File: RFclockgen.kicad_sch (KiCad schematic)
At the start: 13 parts, among them J1 Conn_01x04_Pin, J3 Conn_01x02_Pin, U3 AP2112K-3.3, U4 ESP32-C6-WROOM-1-N8

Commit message: restored to an older version
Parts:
- removed C11: 0.1u, symbol Device:C
- removed C12: 1u, symbol Device:C
- removed R10: 10k, symbol Device:R
- added C2: 10pF, Capacitor_SMD:C_0603_1608Metric_Pad1.08x0.95mm_HandSolder, symbol Device:C
- added R1, R2, R3: 51, Resistor_SMD:R_0603_1608Metric_Pad0.98x0.95mm_HandSolder, symbol Device:R
- added XTAL1: SIT1552AI-JF-DCC-32.768D, BGA4_SiT1532_SIT, symbol 2026-10-07_02-35-18:SIT1552AI-JF-DCC-32.768D
- C5: value 0.1u -> 12p
- C6: value 22u -> 12p
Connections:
- net 3.3V: now also R1.1; no longer C6.1
- net EN: no longer C5.2
- net GND: now also C5.2, R3.2, XTAL1.1 (GND), XTAL1.4 (GND); no longer C5.1
- net at U4.8 (IO0): now also C6.1, XTAL1.2 (CLK_OUT)
- net at U4.9 (IO1): now also C5.1, XTAL1.3 (VDD)
- new net: R1.2, R2.1
- new net: C2.1, R3.1
- new net RF_OUT_A-: C2.2, R2.2
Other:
- removed sheet #PWR020
- added sheet Decoupling capacitors (untitled.kicad_sch)

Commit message: Update
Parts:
- removed C2: 10pF, Capacitor_SMD:C_0603_1608Metric_Pad1.08x0.95mm_HandSolder, symbol Device:C
- removed R1, R2, R3: 51, Resistor_SMD:R_0603_1608Metric_Pad0.98x0.95mm_HandSolder, symbol Device:R
- removed XTAL1: SIT1552AI-JF-DCC-32.768D, BGA4_SiT1532_SIT, symbol 2026-10-07_02-35-18:SIT1552AI-JF-DCC-32.768D
- added C1: 0.1u, symbol Device:C
- added C4: 1u, symbol Device:C
- added R22: 10k, symbol Device:R
- C5: value 12p -> 0.1u
- C6: value 12p -> 22u
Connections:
- net 3.3V: now also C6.1, C1.1, R22.2
- net EN: now also C5.2, C4.1, R22.1
- net GND: now also C5.1, C1.2, C4.2; no longer C5.2
- net at U4.8 (IO0): no longer C6.1
- net at U4.9 (IO1): no longer C5.1
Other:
- removed sheet CrystalOscillator
- removed sheet Decoupling capacitors
- moved on the sheet: C1, C4, FB1, FB2, J1, J3, U3, U4

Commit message: Update
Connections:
- net GND: now also U4.28 (GND), U4.29 (GND), U4.30 (GND), U4.31 (GND), U4.32 (GND), U4.33 (GND), U4.34 (GND), U4.35 (GND), U4.36 (GND), U4.37 (GND)
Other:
- moved on the sheet: C1

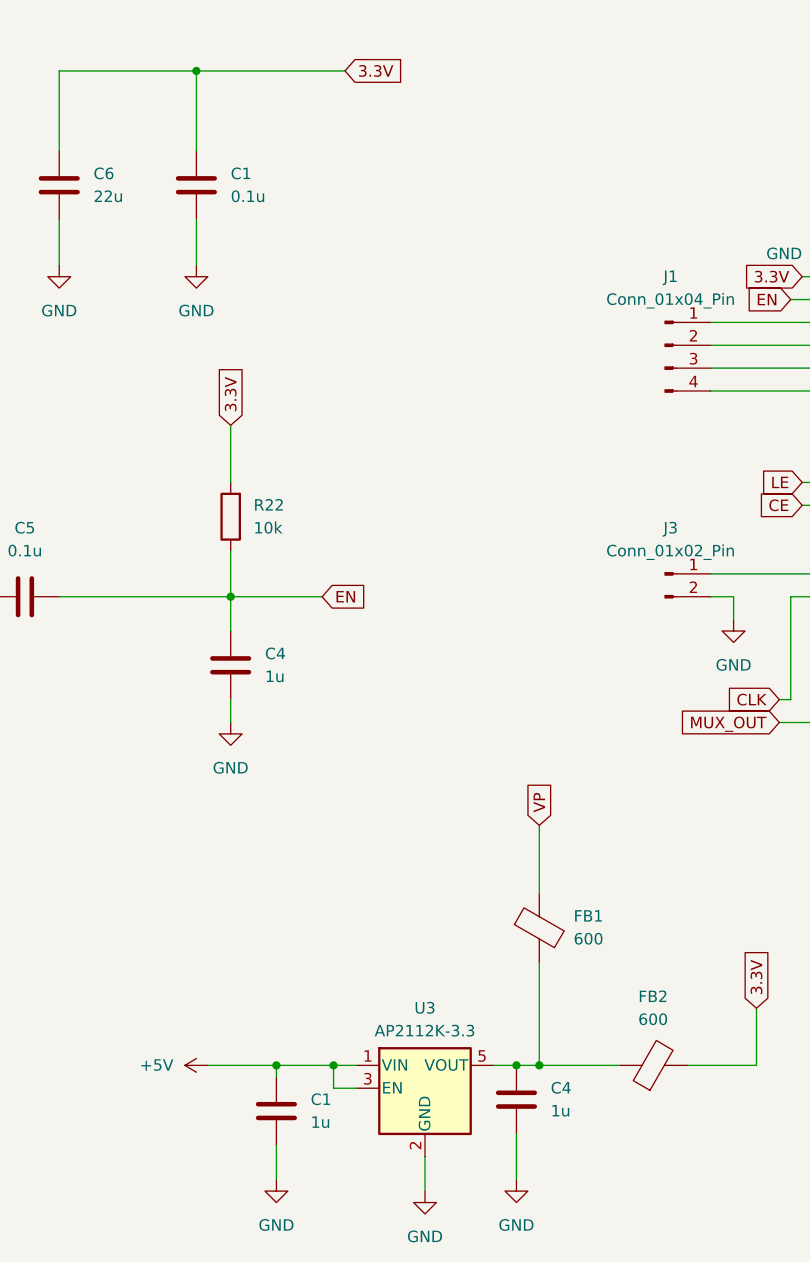
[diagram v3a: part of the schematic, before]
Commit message: Changed overlapping cap ref numbers
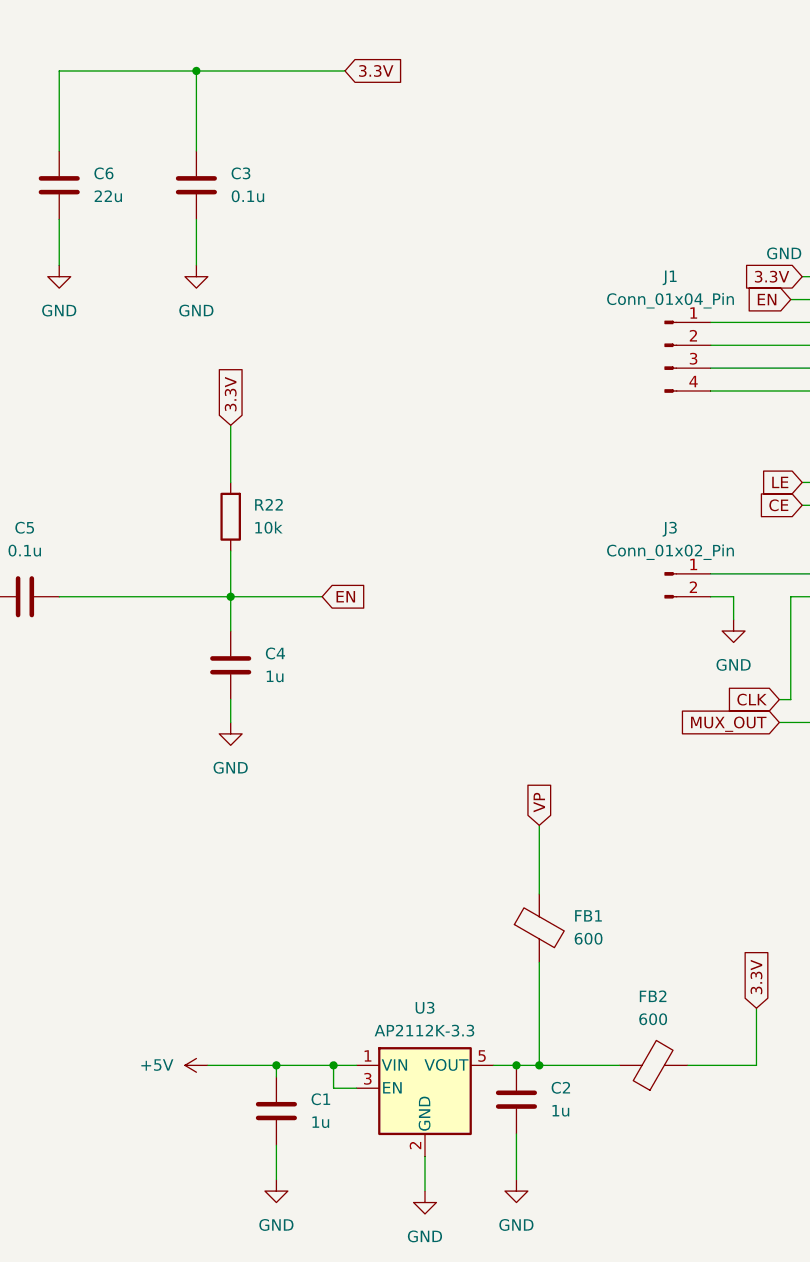
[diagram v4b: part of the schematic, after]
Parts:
- renumbered C4 to C2, C1 to C3
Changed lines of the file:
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@@
 		(dnp no)
 		(fields_autoplaced yes)
-		(property "Reference" "C1"
+		(property "Reference" "C3"
 			(at 101.6 43.1799 0)
 			(effects
@@
 			(project "RFclockgen"
 				(path "/e1444a2d-a0c4-493c-a136-c624dc084e46"
-					(reference "C1")
+					(reference "C3")
 					(unit 1)
 				)
@@
 		(dnp no)
 		(fields_autoplaced yes)
-		(property "Reference" "C4"
+		(property "Reference" "C2"
 			(at 137.16 144.7799 0)
 			(effects
@@
 			(project "RFclockgen"
 				(path "/e1444a2d-a0c4-493c-a136-c624dc084e46"
-					(reference "C4")
-					(unit 1)
-				)
+					(reference "C2")
+					(unit 1)
+				)

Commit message: Changed overlapping R ref numbers
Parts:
- renumbered R22 to R1
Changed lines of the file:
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@@
 		(dnp no)
 		(fields_autoplaced yes)
-		(property "Reference" "R22"
+		(property "Reference" "R1"
 			(at 104.14 80.0099 0)
 			(effects
@@
 			(project "RFclockgen"
 				(path "/e1444a2d-a0c4-493c-a136-c624dc084e46"
-					(reference "R22")
+					(reference "R1")
 					(unit 1)
 				)

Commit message: Changed all Cap footprints to 0805
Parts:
- C1, C2, C3, C4, C5, C6: footprint (none) -> Capacitor_SMD:C_0805_2012Metric_Pad1.18x1.45mm_HandSolder
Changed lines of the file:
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@@
 			)
 		)
-		(property "Footprint" ""
+		(property "Footprint" "Capacitor_SMD:C_0805_2012Metric_Pad1.18x1.45mm_HandSolder"
 			(at 83.5152 48.26 0)
 			(effects
@@
 			)
 		)
-		(property "Footprint" ""
+		(property "Footprint" "Capacitor_SMD:C_0805_2012Metric_Pad1.18x1.45mm_HandSolder"
 			(at 98.7552 48.26 0)
 			(effects
@@
 			)
 		)
-		(property "Footprint" ""
+		(property "Footprint" "Capacitor_SMD:C_0805_2012Metric_Pad1.18x1.45mm_HandSolder"
 			(at 102.5652 101.6 0)
 			(effects
@@
 			)
 		)
-		(property "Footprint" ""
+		(property "Footprint" "Capacitor_SMD:C_0805_2012Metric_Pad1.18x1.45mm_HandSolder"
 			(at 82.55 89.2048 0)
 			(effects
@@
 			)
 		)
-		(property "Footprint" ""
+		(property "Footprint" "Capacitor_SMD:C_0805_2012Metric_Pad1.18x1.45mm_HandSolder"
 			(at 107.6452 151.13 0)
 			(effects
@@
 			)
 		)
-		(property "Footprint" ""
+		(property "Footprint" "Capacitor_SMD:C_0805_2012Metric_Pad1.18x1.45mm_HandSolder"
 			(at 134.3152 149.86 0)
 			(effects

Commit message: Changed all R footprints to 1206
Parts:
- R1: footprint (none) -> Resistor_SMD:R_1206_3216Metric_Pad1.30x1.75mm_HandSolder
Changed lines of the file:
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@@
 			)
 		)
-		(property "Footprint" ""
+		(property "Footprint" "Resistor_SMD:R_1206_3216Metric_Pad1.30x1.75mm_HandSolder"
 			(at 103.378 81.28 90)
 			(effects

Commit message: Actually started on PCB layout
Started the USB C connector
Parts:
- FB1, FB2: footprint (none) -> Inductor_SMD:L_1206_3216Metric_Pad1.22x1.90mm_HandSolder
- J1: footprint (none) -> Connector_PinHeader_1.00mm:PinHeader_1x04_P1.00mm_Vertical
- J3: footprint (none) -> Connector_PinHeader_1.00mm:PinHeader_1x02_P1.00mm_Vertical
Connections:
- net UART_RXD: now reaches U4.24 (RXD0)
- net UART_TXD: now reaches U4.25 (TXD0)
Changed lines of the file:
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@@
+		)
+	)
+	(global_label "UART_RXD"
+		(shape input)
+		(at 209.55 85.09 0)
+		(fields_autoplaced yes)
+		(effects
+			(font
+				(size 1.27 1.27)
+			)
+			(justify left)
+		)
+		(property "Intersheetrefs" "${INTERSHEET_REFS}"
+			(at 221.909 85.09 0)
+			(effects
+				(font
+					(size 1.27 1.27)
+				)
+				(justify left)
+				(hide yes)
+			)
 		)
 	)
@@
 		)
 	)
+	(global_label "UART_TXD"
+		(shape input)
+		(at 209.55 82.55 0)
+		(fields_autoplaced yes)
+		(effects
+			(font
+				(size 1.27 1.27)
+			)
+			(justify left)
+		)
+		(property "Intersheetrefs" "${INTERSHEET_REFS}"
+			(at 221.6066 82.55 0)
+			(effects
+				(font
+					(size 1.27 1.27)
+				)
+				(justify left)
+				(hide yes)
+			)
+		)
+	)
 	(symbol
 		(lib_id "power:GND")
@@
 			)
 		)
-		(property "Footprint" ""
+		(property "Footprint" "Connector_PinHeader_1.00mm:PinHeader_1x04_P1.00mm_Vertical"
 			(at 149.86 62.23 0)
 			(effects
@@
 			)
 		)
-		(property "Footprint" ""
+		(property "Footprint" "Inductor_SMD:L_1206_3216Metric_Pad1.22x1.90mm_HandSolder"
 			(at 148.59 144.018 90)
 			(effects
@@
 			)
 		)
-		(property "Footprint" ""
+		(property "Footprint" "Connector_PinHeader_1.00mm:PinHeader_1x02_P1.00mm_Vertical"
 			(at 149.86 87.63 0)
 			(effects
@@
 			)
 		)
-		(property "Footprint" ""
+		(property "Footprint" "Inductor_SMD:L_1206_3216Metric_Pad1.22x1.90mm_HandSolder"
 			(at 134.112 127 90)
 			(effects
